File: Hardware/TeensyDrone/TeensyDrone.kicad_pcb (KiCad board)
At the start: 2 copper layers, 30 x 90 mm, 16 parts, among them J1 Conn_01x04, J2 Conn_01x08, J3 Conn_01x04, U1 DEV-15583

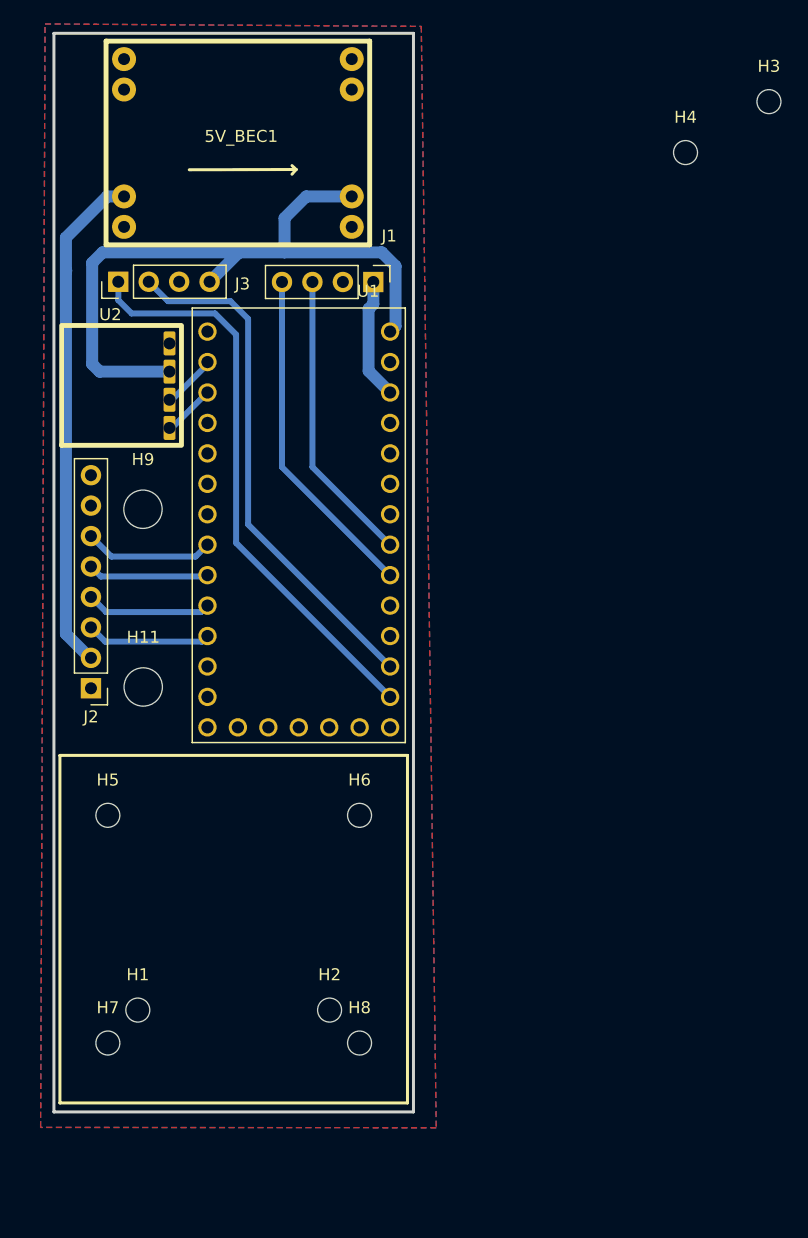
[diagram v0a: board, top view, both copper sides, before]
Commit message: Revert "Moved to Teensy 4.0 from 4.1"
This reverts commit 64f42becbd12878e856e1dc259d1d069ff850610.
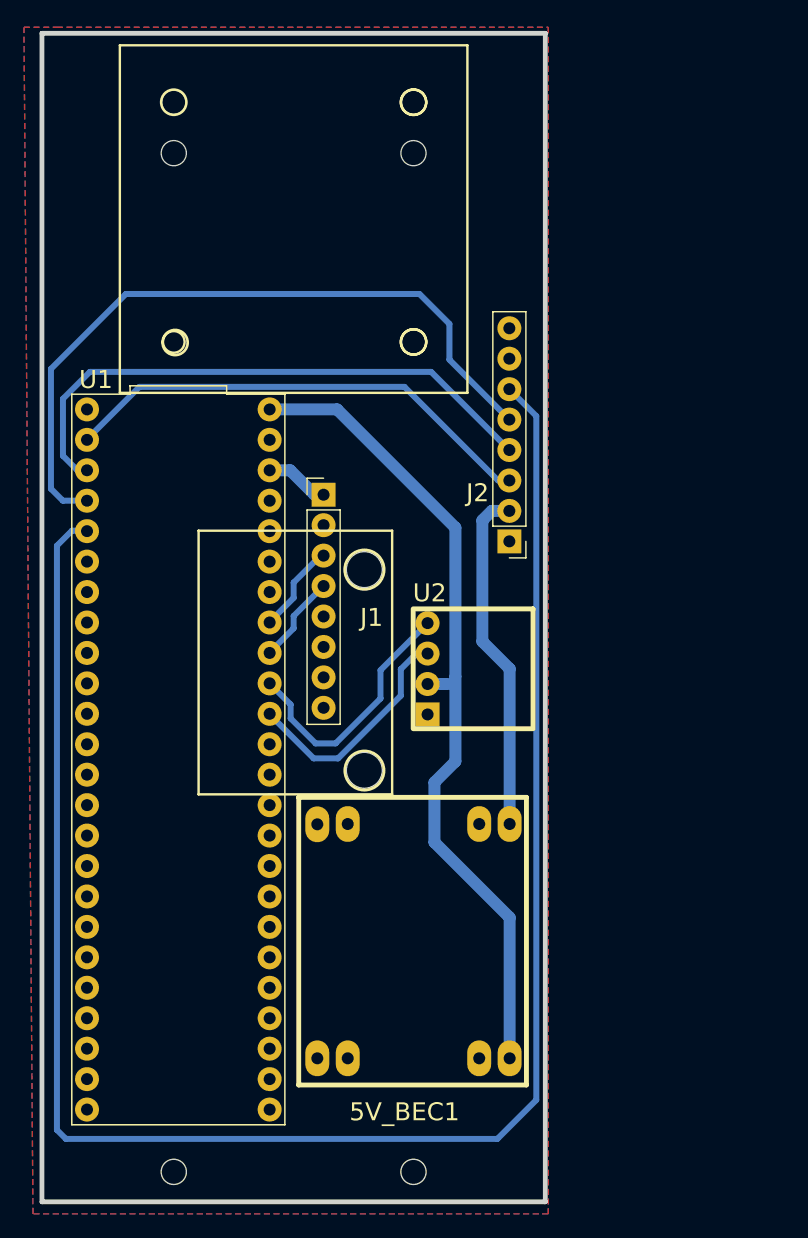
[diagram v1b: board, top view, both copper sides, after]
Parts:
- removed H1, H2, H3, H4, H5, H6, H7, H8: MountingHole, MountingHole:MountingHole_2mm
- removed H11, H9: MountingHole, MountingHole:MountingHole_3.2mm_M3
- removed J3: Conn_01x04, Connector_PinHeader_2.54mm:PinHeader_1x04_P2.54mm_Vertical
- added MountHole1: MountingHole_2.1mm, MountingHole:MountingHole_2.1mm, F.Cu at (35.0, 35.0)
- added MountHole2: MountingHole_2.1mm, MountingHole:MountingHole_2.1mm, F.Cu at (55.0, 35.0)
- added MountHole3: MountingHole_2.1mm, MountingHole:MountingHole_2.1mm, F.Cu at (35.0, 120.0)
- added MountHole4: MountingHole_2.1mm, MountingHole:MountingHole_2.1mm, F.Cu at (55.0, 120.0)
- added MountingHoleAcc1: , clipboard:ab9ca41b-535c-4e5d-965d-18f4c74ecc4b, F.Cu at (50.9, 68.1)
- added MountingHoleAcc2: , clipboard:ab9ca41b-535c-4e5d-965d-18f4c74ecc4b, F.Cu at (50.9, 84.9)
- added Mounting_hole_esc_1: MNT, clipboard:cc0a7048-0dbf-4480-81d8-83834bec2c2a, F.Cu at (35.0, 28.5)
- added Mounting_hole_esc_2: MNT, clipboard:cc0a7048-0dbf-4480-81d8-83834bec2c2a, F.Cu at (35.1, 48.5)
- added Mounting_hole_esc_3: MNT, clipboard:cc0a7048-0dbf-4480-81d8-83834bec2c2a, F.Cu at (55.0, 48.5)
- added Mounting_hole_esc_4: MNT, clipboard:cc0a7048-0dbf-4480-81d8-83834bec2c2a, F.Cu at (55.0, 28.5)
- J1: value Conn_01x04 -> Conn_01x08; footprint Connector_PinHeader_2.54mm:PinHeader_1x04_P2.54mm_Vertical -> Connector_PinHeader_2.54mm:PinHeader_1x08_P2.54mm_Vertical
- U1: value DEV-15583 -> DEV-16771; footprint DEV-15583:MODULE_DEV-15583 -> Teensy 4.1:MODULE_DEV-16771
- moved 5V_BEC1 79.3 mm to (55.0, 100.7), turned to -90 degrees
- moved U2 41.6 mm to (65.0, 73.0), turned to -90 degrees
- moved J2 37.0 mm to (63.0, 67.4)
- moved U1 21.7 mm to (35.4, 85.6), turned to -90 degrees
- moved J1 18.2 mm to (47.5, 63.5), turned to 0 degrees
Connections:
- 5V_BEC1 pad 1: GND -> Net-(J2-VBat)
- 5V_BEC1 pad 3: Net-(J2-VBat) -> GND
- 5V_BEC1 pad 5: GND -> 5V
- 5V_BEC1 pad 7: Net-(J3-5V) -> GND
- J2 pad 3: Net-(J2-Pin_3) -> Net-(J2-Servo1)
- J2 pad 4: Net-(J2-Pin_4) -> Net-(J2-Servo2)
- J2 pad 5: Net-(J2-Pin_5) -> Net-(J2-Servo3)
- J2 pad 6: Net-(J2-Pin_6) -> Net-(J2-Servo4)
- U1 pad 0: Net-(U2-TX) -> Net-(J2-Servo1)
- U1 pad 1: Net-(U2-RX) -> Net-(J2-Servo2)
- U1 pad 14: Net-(J3-RX) -> unconnected-(U1-A0-Pad14)
- U1 pad 15: Net-(J3-TX) -> unconnected-(U1-A1-Pad15)
- U1 pad 16: unconnected-(U1-Pad16) -> Net-(U2-TX)
- U1 pad 17: unconnected-(U1-Pad17) -> Net-(U2-RX)
- U1 pad 2: unconnected-(U1-Pad2) -> Net-(J2-Servo3)
- U1 pad 3: unconnected-(U1-Pad3) -> Net-(J2-Servo4)
- U1 pad 6: Net-(J2-Pin_6) -> unconnected-(U1-OUT1D-Pad6)
- U1 pad 7: Net-(J2-Pin_5) -> unconnected-(U1-RX2-Pad7)
- U1 pad 8: Net-(J2-Pin_4) -> unconnected-(U1-TX2-Pad8)
- U1 pad 9: Net-(J2-Pin_3) -> unconnected-(U1-OUT1C-Pad9)
- U2 pad 2: Net-(J3-5V) -> 5V
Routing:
- net Net-(J2-Servo4): track 0.00 -> 153.6 mm
- net 5V: track 0.00 -> 69.0 mm
- net Net-(J2-Servo3): track 0.00 -> 60.3 mm
- net Net-(J3-5V): track 59.6 -> 0.00 mm
- net Net-(J3-RX): track 48.1 -> 0.00 mm
- net Net-(J2-Servo2): track 0.00 -> 48.1 mm
- net Net-(J3-TX): track 43.5 -> 0.00 mm
- net Net-(J2-Servo1): track 0.00 -> 40.4 mm
- net Net-(J1-SDA): track 28.2 -> 7.46 mm
- net Net-(U2-RX): track 4.39 -> 21.8 mm
- net Net-(J1-SCL): track 24.6 -> 7.36 mm
- net Net-(U2-TX): track 4.58 -> 19.7 mm
- net Net-(J2-VBat): track 42.3 -> 28.9 mm
- net Net-(J2-Pin_6): track 10.8 -> 0.00 mm
- net Net-(J2-Pin_4): track 10.5 -> 0.00 mm
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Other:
- board size 30 x 90 mm -> 42 x 97.5 mm
- board text removed: "Board Cutout : 90mm x 30mm"
- board text removed: "ESC Outline Mounted on Gummies above"
- board text removed: "End of Drone"
- board text removed: "Front of Drone"
- board text removed: "IMU + ESC Both Not On Board, Mounted Above"
